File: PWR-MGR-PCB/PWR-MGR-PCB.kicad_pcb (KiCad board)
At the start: 2 copper layers, 32 x 37.4 mm, 20 parts, among them J1 USB_C_Receptacle_USB2.0_14P, J2 Battery_1x2, U1 USBLC6-2SC6, U2 TLV75533PDBV, U3 BQ24074RGT

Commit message: Refine outline
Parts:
- moved U3 3.71 mm to (161.9, 82.8)
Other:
- board size 32 x 37.4 mm -> 30 x 35 mm
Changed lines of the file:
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@@
 	(footprint "BQ24074RGTR:QFN50P300X300X100-17N"
 		(layer "F.Cu")
-		(at 165.239 84.493)
+		(at 161.913 82.842)
 		(property "Reference" "U3"
 			(at -0.165 -3.24 0)
@@
 		)
 	)
-	(gr_line
-		(start 141.3256 74.3712)
-		(end 141.3256 111.76)
+	(gr_arc
+		(start 140 82)
+		(mid 140.585786 80.585786)
+		(end 142 80)
 		(stroke
 			(width 0.05)
@@
 	)
 	(gr_line
-		(start 173.3296 74.3712)
-		(end 141.3256 74.3712)
+		(start 142 115)
+		(end 168 115)
 		(stroke
 			(width 0.05)
@@
 	)
 	(gr_line
-		(start 141.3256 111.76)
-		(end 173.3296 111.76)
+		(start 140 82)
+		(end 140 113)
 		(stroke
 			(width 0.05)
@@
 	)
 	(gr_line
-		(start 173.3296 111.76)
-		(end 173.3296 74.3712)
+		(start 170 113)
+		(end 170 82)
 		(stroke
 			(width 0.05)
+			(type default)
+		)
+		(layer "Edge.Cuts")
+	)
+	(gr_arc
+		(start 142 115)
+		(mid 140.585786 114.414214)
+		(end 140 113)
+		(stroke
+			(width 0.05)
+			(type default)
+		)
+		(layer "Edge.Cuts")
+	)
+	(gr_line
+		(start 168 80)
+		(end 142 80)
+		(stroke
+			(width 0.05)
+			(type default)
+		)
+		(layer "Edge.Cuts")
+	)
+	(gr_arc
+		(start 168 80)
+		(mid 169.414214 80.585786)
+		(end 170 82)
+		(stroke
+			(width 0.05)
+			(type default)
+		)
+		(layer "Edge.Cuts")
+	)
+	(gr_arc
+		(start 170 113)
+		(mid 169.414214 114.414214)
+		(end 168 115)
+		(stroke
+			(width 0.05)

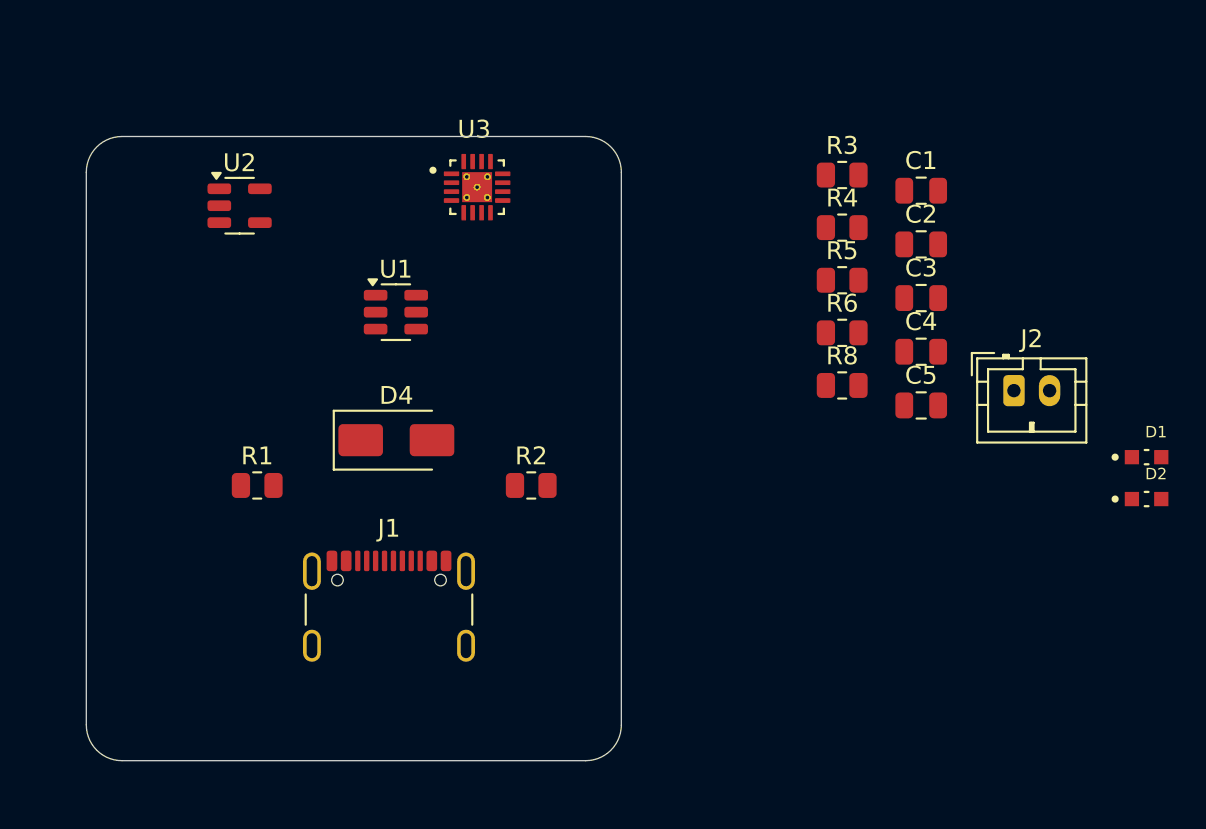
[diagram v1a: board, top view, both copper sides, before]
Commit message: Start placement
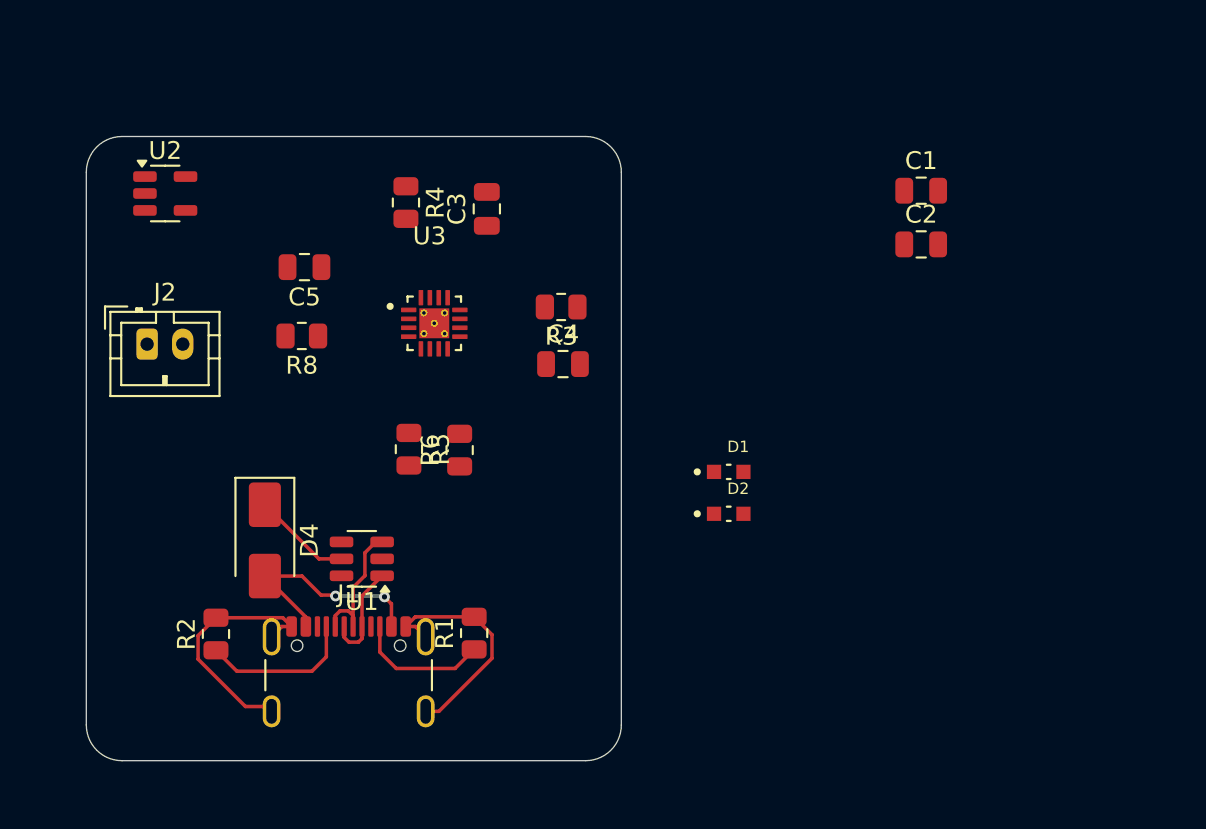
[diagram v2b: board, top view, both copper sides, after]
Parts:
- moved J2 48.7 mm to (143.4, 91.6)
- moved C5 35.4 mm to (152.2, 87.3), turned to 180 degrees
- moved R8 30.4 mm to (152.1, 91.2), turned to 180 degrees
- moved R5 26.1 mm to (158.1, 97.5), turned to 90 degrees
- moved C3 24.9 mm to (162.5, 84.1), turned to 90 degrees
- moved R4 24.5 mm to (157.9, 83.7), turned to -90 degrees
- moved D1 23.4 mm to (176.0, 98.8)
- moved D2 23.4 mm to (176.0, 101.2)
- moved R6 22.4 mm to (160.9, 97.6), turned to 90 degrees
- moved C4 20.1 mm to (166.7, 92.8)
- moved R2 19.5 mm to (147.3, 107.9), turned to 90 degrees
- moved R3 17.4 mm to (166.6, 89.6), turned to 180 degrees
- moved R1 14.7 mm to (161.7, 107.8), turned to 90 degrees
- moved U1 14.0 mm to (155.4, 103.7), turned to 180 degrees
- moved D4 9.27 mm to (150.0, 102.6), turned to -90 degrees
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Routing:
- net GND: track 0.00 -> 27.0 mm
- net Net-(D4-A): track 0.00 -> 12.8 mm, vias 0 -> 2
- net Net-(J1-CC1): track 0.00 -> 8.71 mm
- net /USB_CONN_D-: track 0.00 -> 8.06 mm
- net Net-(J1-CC2): track 0.00 -> 7.55 mm
- net /USB_CONN_D+: track 0.00 -> 5.79 mm
- net VBUS 5V: track 0.00 -> 5.56 mm

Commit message: Start bq2407 zones
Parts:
- moved C4 4.75 mm to (162.0, 93.0), turned to -90 degrees
- moved R3 3.51 mm to (167.2, 86.1)
- moved U3 2.62 mm to (157.3, 92.0)
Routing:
- added copper zone on F.Cu, net VCC_BMS
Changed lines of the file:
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@@
 	(footprint "Resistor_SMD:R_0805_2012Metric"
 		(layer "F.Cu")
-		(at 166.6259 89.5604 180)
+		(at 167.2 86.1 180)
 		(descr "Resistor SMD 0805 (2012 Metric), square (rectangular) end terminal, IPC-7351 nominal, (Body size source: IPC-SM-782 page 72, https://www.pcb-3d.com/wordpress/wp-content/uploads/ipc-sm-782a_amendment_1_and_2.pdf), generated with kicad-footprint-generator")
 		(tags "resistor")
@@
 	(footprint "Capacitor_SMD:C_0805_2012Metric"
 		(layer "F.Cu")
-		(at 166.7294 92.7608)
+		(at 161.988 92.9752 -90)
 		(descr "Capacitor SMD 0805 (2012 Metric), square (rectangular) end terminal, IPC-7351 nominal, (Body size source: IPC-SM-782 page 76, https://www.pcb-3d.com/wordpress/wp-content/uploads/ipc-sm-782a_amendment_1_and_2.pdf, https://docs.google.com/spreadsheets/d/1BsfQQcO9C6DZCsRaXUlFlo91Tg2WpOkGARC1WS5S8t0/edit?usp=sharing), generated with kicad-footprint-generator")
 		(tags "capacitor")
 		(property "Reference" "C4"
-			(at 0 -1.68 0)
+			(at 0 -1.68 90)
 			(layer "F.SilkS")
 			(effects
@@
 		)
 		(property "Value" "4.7uF"
-			(at 0 1.68 0)
+			(at 0 1.55 90)
 			(layer "F.Fab")
 			(effects
@@
 		)
 		(property "Datasheet" "~"
-			(at 0 0 0)
+			(at 0 0 90)
 			(layer "F.Fab")
 			(hide yes)
@@
 		)
 		(property "Description" "Unpolarized capacitor"
-			(at 0 0 0)
+			(at 0 0 90)
 			(layer "F.Fab")
 			(hide yes)
@@
 		(attr smd)
 		(fp_line
-			(start -0.261252 -0.735)
-			(end 0.261252 -0.735)
+			(start -0.261252 0.735)
+			(end 0.261252 0.735)
 			(stroke
 				(width 0.12)
@@
 		)
 		(fp_line
-			(start -0.261252 0.735)
-			(end 0.261252 0.735)
+			(start -0.261252 -0.735)
+			(end 0.261252 -0.735)
 			(stroke
 				(width 0.12)
@@
 		)
 		(fp_line
-			(start -1.7 -0.98)
-			(end 1.7 -0.98)
+			(start -1.7 0.98)
+			(end -1.7 -0.98)
 			(stroke
 				(width 0.05)
@@
 		)
 		(fp_line
-			(start -1.7 0.98)
-			(end -1.7 -0.98)
+			(start 1.7 0.98)
+			(end -1.7 0.98)
 			(stroke
 				(width 0.05)
@@
 		)
 		(fp_line
-			(start 1.7 -0.98)
-			(end 1.7 0.98)
+			(start -1.7 -0.98)
+			(end 1.7 -0.98)
 			(stroke
 				(width 0.05)
@@
 		)
 		(fp_line
-			(start 1.7 0.98)
-			(end -1.7 0.98)
+			(start 1.7 -0.98)
+			(end 1.7 0.98)
 			(stroke
 				(width 0.05)
@@
 		)
 		(fp_line
-			(start -1 -0.625)
-			(end 1 -0.625)
+			(start -1 0.625)
+			(end -1 -0.625)
 			(stroke
 				(width 0.1)
@@
 		)
 		(fp_line
-			(start -1 0.625)
-			(end -1 -0.625)
+			(start 1 0.625)
+			(end -1 0.625)
 			(stroke
 				(width 0.1)
@@
 		)
 		(fp_line
-			(start 1 -0.625)
-			(end 1 0.625)
+			(start -1 -0.625)
+			(end 1 -0.625)
 			(stroke
 				(width 0.1)
@@
 		)
 		(fp_line
-			(start 1 0.625)
-			(end -1 0.625)
+			(start 1 -0.625)
+			(end 1 0.625)
 			(stroke
 				(width 0.1)
@@
 		)
 		(fp_text user "${REFERENCE}"
-			(at 0 0 0)
+			(at 0 0 90)
 			(layer "F.Fab")
 			(effects
@@
 		)
 		(pad "1" smd roundrect
-			(at -0.95 0)
+			(at -0.95 0 270)
 			(size 1 1.45)
 			(layers "F.Cu" "F.Mask" "F.Paste")
@@
 		)
 		(pad "2" smd roundrect
-			(at 0.95 0)
+			(at 0.95 0 270)
 			(size 1 1.45)
 			(layers "F.Cu" "F.Mask" "F.Paste")
@@
 	(footprint "BQ24074RGTR:QFN50P300X300X100-17N"
 		(layer "F.Cu")
-		(at 159.512 90.4748)
+		(at 157.35 91.95)
 		(property "Reference" "U3"
 			(at -0.2698 -4.8934 0)
@@
 		(net 16)
 	)
+	(zone
+		(net 1)
+		(net_name "VCC_BMS")
+		(layer "F.Cu")
+		(hatch edge 0.5)
+		(connect_pads
+			(clearance 0.1)
+		)
+		(min_thickness 0.1)
+		(filled_areas_thickness no)
+		(fill yes
+			(thermal_gap 0.2)
+			(thermal_bridge_width 0.5)
+		)
+		(polygon
+			(pts
+				(xy 158.338 91.4752) (xy 158.338 92.4252) (xy 160.388 92.4252) (xy 160.888 92.8752) (xy 163.338 92.8752)
+				(xy 163.338 90.9752) (xy 160.838 90.9752) (xy 160.338 91.4752)
+			)
+		)
+	)
 	(embedded_fonts no)

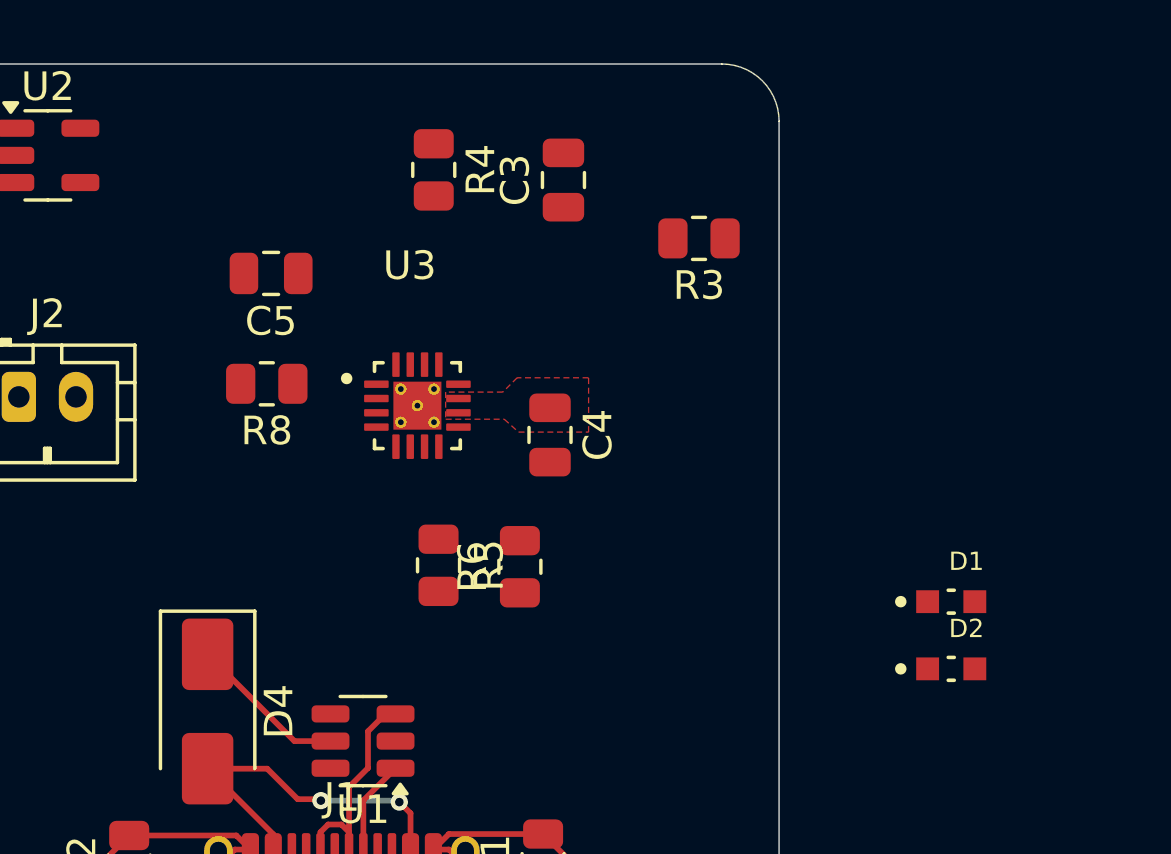
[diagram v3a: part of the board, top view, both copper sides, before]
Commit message: Add filled zones around battery charger
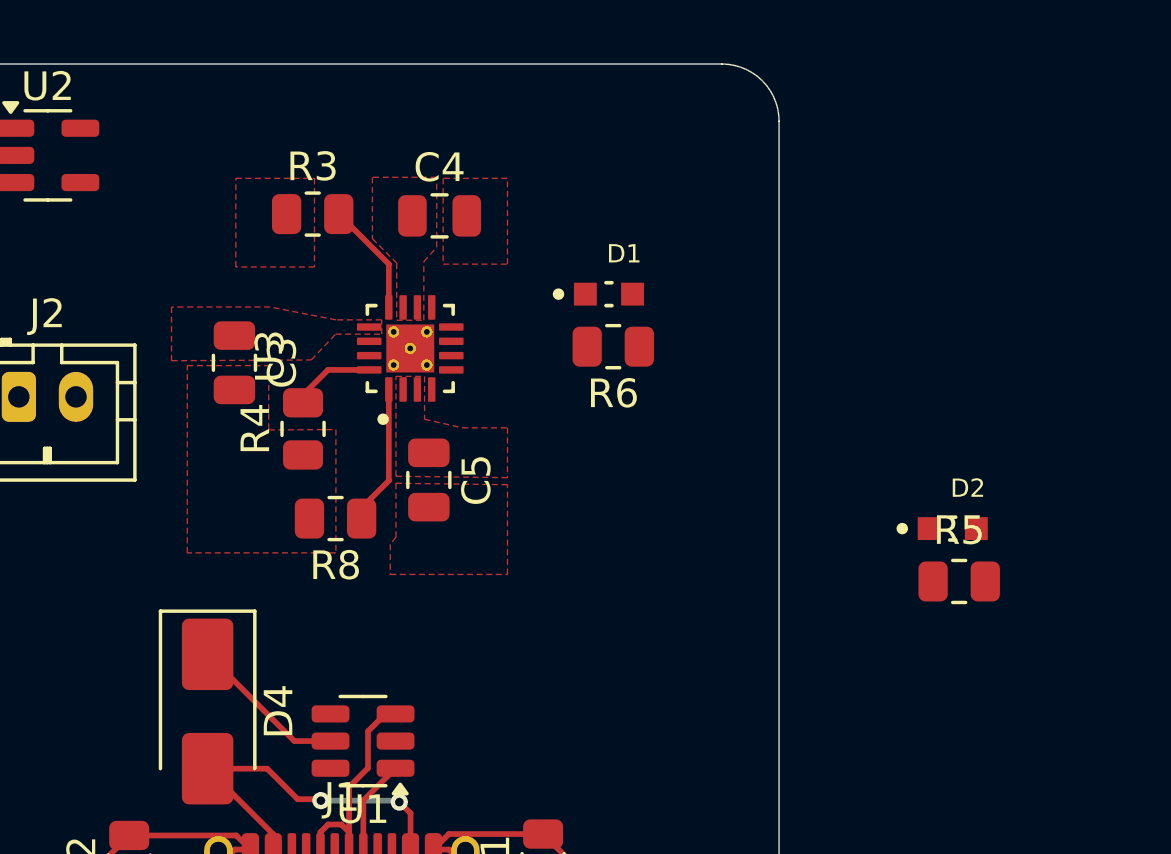
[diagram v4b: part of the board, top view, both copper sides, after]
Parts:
- moved R5 18.2 mm to (176.3, 98.1), turned to 180 degrees
- moved D1 16.1 mm to (164.1, 88.0)
- moved R3 13.5 mm to (153.7, 85.2), turned to 0 degrees
- moved C3 13.2 mm to (150.9, 90.5), turned to -90 degrees
- moved R4 10.1 mm to (153.3, 92.8), turned to 90 degrees
- moved C5 9.09 mm to (157.8, 94.5), turned to -90 degrees
- moved C4 8.58 mm to (158.1, 85.3), turned to 0 degrees
- moved R6 8.36 mm to (164.2, 89.9), turned to 180 degrees
- moved R8 5.29 mm to (154.5, 95.9)
- moved D2 4.91 mm to (176.1, 96.2)
- moved U3 2.02 mm to (157.1, 90.0), turned to 90 degrees
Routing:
- net Net-(U3-TS): track 0.00 -> 5.06 mm
- net Net-(U3-ILIM): track 0.00 -> 3.99 mm
- net Net-(U3-ISET): track 0.00 -> 3.10 mm
- added copper zone on F.Cu, net /V_BATT
- added copper zone on F.Cu, net GND
- added copper zone on F.Cu, net VBUS 5V

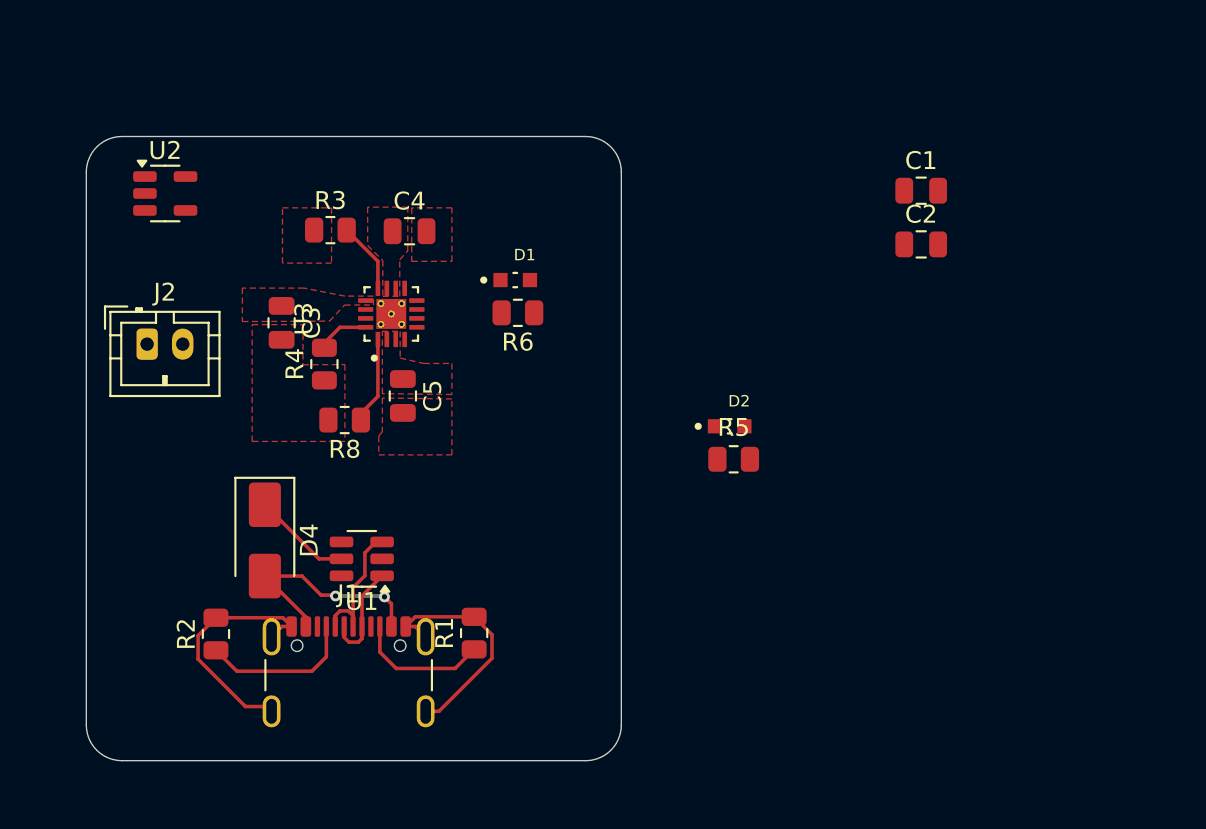
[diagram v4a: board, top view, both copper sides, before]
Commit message: Add power LEDs, connect battery terminal
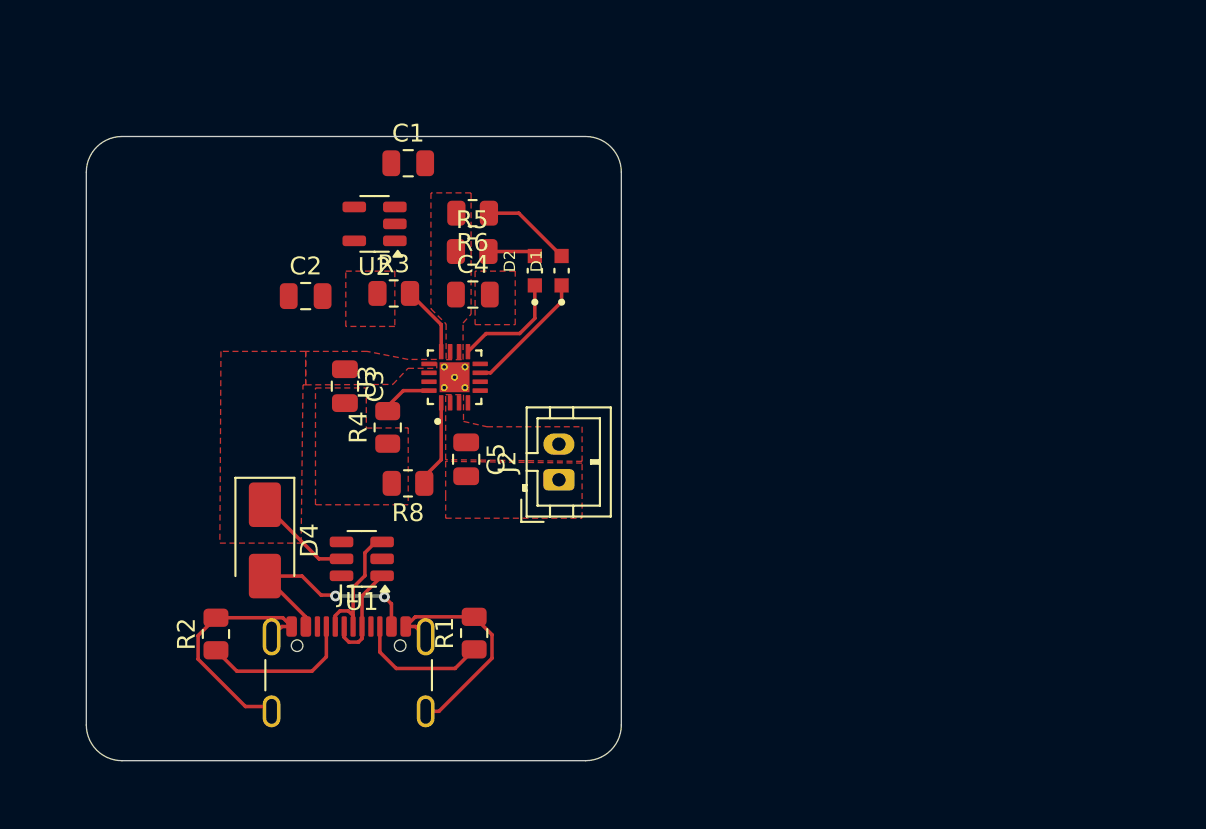
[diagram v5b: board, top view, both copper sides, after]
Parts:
- moved C2 34.6 mm to (152.3, 89.0)
- moved C1 28.8 mm to (158.1, 81.5)
- moved J2 24.3 mm to (166.5, 99.2), turned to 90 degrees
- moved R5 18.7 mm to (161.6, 86.5)
- moved D2 14.0 mm to (165.2, 87.5), turned to 90 degrees
- moved U2 11.9 mm to (156.2, 84.9), turned to 180 degrees
- moved R6 6.14 mm to (161.7, 84.3)
- moved C3 5.02 mm to (154.5, 94.0)
- moved C5 5.02 mm to (161.3, 98.1)
- moved R3 5.02 mm to (157.2, 88.8)
- moved R4 5.02 mm to (156.9, 96.3)
- moved U3 5.02 mm to (160.7, 93.5)
- moved C4 5.02 mm to (161.7, 88.9)
- moved R8 5.02 mm to (158.0, 99.5)
- moved D1 2.65 mm to (166.7, 87.5), turned to 90 degrees
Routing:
- net Net-(U3-~{PGOOD}): track 0.00 -> 7.13 mm
- net Net-(U3-~{CHG}): track 0.00 -> 6.40 mm
- net Net-(D1-PadA): track 0.00 -> 5.07 mm
- net Net-(D2-PadA): track 0.00 -> 3.02 mm
